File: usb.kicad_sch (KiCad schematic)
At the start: 6 parts, among them J4 USB_C_Receptacle_USB2.0, U4 PTN5150AHXMP

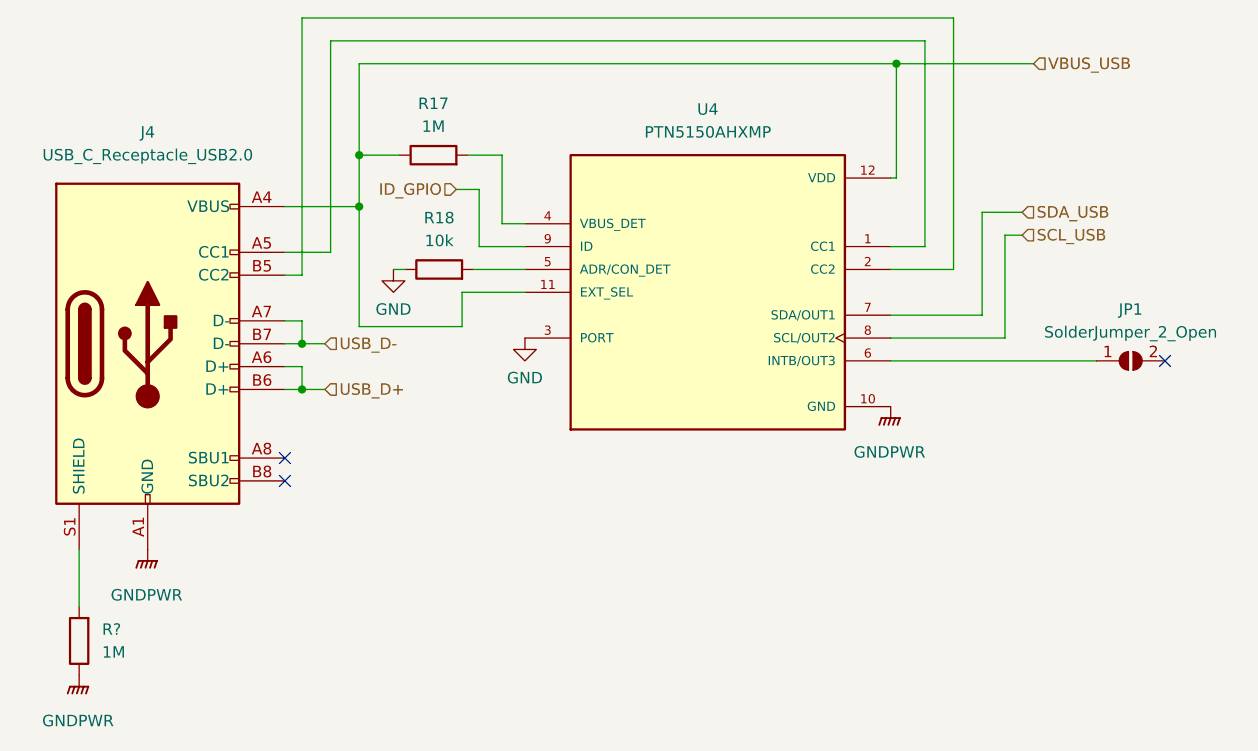
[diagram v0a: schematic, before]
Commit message: USB IC Removal
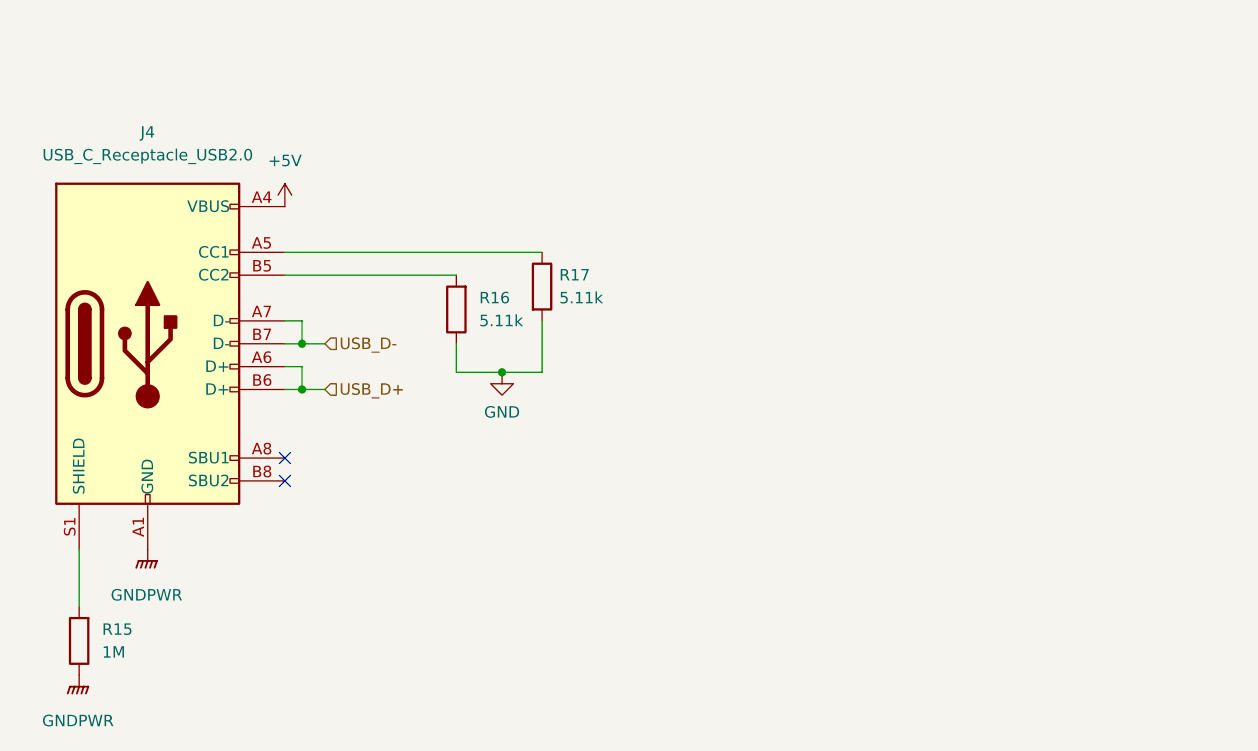
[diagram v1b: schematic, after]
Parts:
- removed JP1: SolderJumper_2_Open, Jumper:SolderJumper-2_P1.3mm_Open_Pad1.0x1.5mm, symbol Jumper:SolderJumper_2_Open
- removed R18: 10k, Resistor_SMD:R_0402_1005Metric, symbol Device:R
- removed U4: PTN5150AHXMP, JLCPCB:IC_PTN5150AHXMP, symbol JLCPCB:PTN5150AHXMP
- added R16: 5.11k, Resistor_SMD:R_0402_1005Metric, symbol Device:R
- R17: value 1M -> 5.11k
- gave numbers to parts that had none: 1
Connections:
- net GND: now also R17.2, R16.1
- net at J4.A5 (CC1): now also R17.1
- net at J4.B5 (CC2): now also R16.2
- net VBUS_USB renamed +5V
- net +5V: no longer R17.1
- no-connect marks 3 -> 2

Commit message: All Routed!
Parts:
- J6: renamed from J4; footprint JLCPCB:SOFNG_MC-311D -> lib_fp:SOFNG_MC-311D; MPN (none) -> C136423
- renumbered R15 to R17, R16 to R18, R17 to R19
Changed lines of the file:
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@@
   (symbol (lib_id "power:+5V") (at 128.905 72.39 0) (unit 1)
     (in_bom yes) (on_board yes) (fields_autoplaced)
-    (property "Reference" "#PWR033" (id 0) (at 128.905 76.2 0)
+    (property "Reference" "#PWR043" (id 0) (at 128.905 76.2 0)
       (effects (font (size 1.27 1.27)) hide)
     )
@@
   (symbol (lib_id "power:GND") (at 153.035 90.805 0) (unit 1)
     (in_bom yes) (on_board yes) (fields_autoplaced)
-    (property "Reference" "#PWR034" (id 0) (at 153.035 97.155 0)
+    (property "Reference" "#PWR044" (id 0) (at 153.035 97.155 0)
       (effects (font (size 1.27 1.27)) hide)
     )
@@
   (symbol (lib_id "Device:R") (at 106.045 120.65 180) (unit 1)
     (in_bom yes) (on_board yes) (fields_autoplaced)
-    (property "Reference" "R15" (id 0) (at 108.585 119.3799 0)
+    (property "Reference" "R17" (id 0) (at 108.585 119.3799 0)
       (effects (font (size 1.27 1.27)) (justify right))
     )
@@
   (symbol (lib_id "Device:R") (at 157.48 81.28 0) (unit 1)
     (in_bom yes) (on_board yes) (fields_autoplaced)
-    (property "Reference" "R17" (id 0) (at 159.385 80.0099 0)
+    (property "Reference" "R19" (id 0) (at 159.385 80.0099 0)
       (effects (font (size 1.27 1.27)) (justify left))
     )
@@
   (symbol (lib_id "power:GNDPWR") (at 113.665 110.49 0) (unit 1)
     (in_bom yes) (on_board yes) (fields_autoplaced)
-    (property "Reference" "#PWR032" (id 0) (at 113.665 115.57 0)
+    (property "Reference" "#PWR042" (id 0) (at 113.665 115.57 0)
       (effects (font (size 1.27 1.27)) hide)
     )
@@
   (symbol (lib_id "power:GNDPWR") (at 106.045 124.46 0) (unit 1)
     (in_bom yes) (on_board yes) (fields_autoplaced)
-    (property "Reference" "#PWR031" (id 0) (at 106.045 129.54 0)
+    (property "Reference" "#PWR041" (id 0) (at 106.045 129.54 0)
       (effects (font (size 1.27 1.27)) hide)
     )
@@
   (symbol (lib_id "Connector:USB_C_Receptacle_USB2.0") (at 113.665 87.63 0) (unit 1)
     (in_bom yes) (on_board yes) (fields_autoplaced)
-    (property "Reference" "J4" (id 0) (at 113.665 64.135 0))
+    (property "Reference" "J6" (id 0) (at 113.665 64.135 0))
     (property "Value" "USB_C_Receptacle_USB2.0" (id 1) (at 113.665 66.675 0))
-    (property "Footprint" "JLCPCB:SOFNG_MC-311D" (id 2) (at 117.475 87.63 0)
+    (property "Footprint" "lib_fp:SOFNG_MC-311D" (id 2) (at 117.475 87.63 0)
       (effects (font (size 1.27 1.27)) hide)
     )
     (property "Datasheet" "https://www.usb.org/sites/default/files/documents/usb_type-c.zip" (id 3) (at 117.475 87.63 0)
+      (effects (font (size 1.27 1.27)) hide)
+    )
+    (property "MPN" "C136423" (id 4) (at 113.665 87.63 0)
       (effects (font (size 1.27 1.27)) hide)
     )
@@
   (symbol (lib_id "Device:R") (at 147.955 83.82 180) (unit 1)
     (in_bom yes) (on_board yes) (fields_autoplaced)
-    (property "Reference" "R16" (id 0) (at 150.495 82.5499 0)
+    (property "Reference" "R18" (id 0) (at 150.495 82.5499 0)
       (effects (font (size 1.27 1.27)) (justify right))
     )

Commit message: New Audio
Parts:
- renumbered R17 to R15, R18 to R16, R19 to R17
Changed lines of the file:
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@@
   (symbol (lib_id "power:+5V") (at 128.905 72.39 0) (unit 1)
     (in_bom yes) (on_board yes) (fields_autoplaced)
-    (property "Reference" "#PWR043" (id 0) (at 128.905 76.2 0)
+    (property "Reference" "#PWR044" (id 0) (at 128.905 76.2 0)
       (effects (font (size 1.27 1.27)) hide)
     )
@@
   (symbol (lib_id "power:GND") (at 153.035 90.805 0) (unit 1)
     (in_bom yes) (on_board yes) (fields_autoplaced)
-    (property "Reference" "#PWR044" (id 0) (at 153.035 97.155 0)
+    (property "Reference" "#PWR045" (id 0) (at 153.035 97.155 0)
       (effects (font (size 1.27 1.27)) hide)
     )
@@
   (symbol (lib_id "Device:R") (at 106.045 120.65 180) (unit 1)
     (in_bom yes) (on_board yes) (fields_autoplaced)
-    (property "Reference" "R17" (id 0) (at 108.585 119.3799 0)
+    (property "Reference" "R15" (id 0) (at 108.585 119.3799 0)
       (effects (font (size 1.27 1.27)) (justify right))
     )
@@
   (symbol (lib_id "Device:R") (at 157.48 81.28 0) (unit 1)
     (in_bom yes) (on_board yes) (fields_autoplaced)
-    (property "Reference" "R19" (id 0) (at 159.385 80.0099 0)
+    (property "Reference" "R17" (id 0) (at 159.385 80.0099 0)
       (effects (font (size 1.27 1.27)) (justify left))
     )
@@
   (symbol (lib_id "power:GNDPWR") (at 113.665 110.49 0) (unit 1)
     (in_bom yes) (on_board yes) (fields_autoplaced)
-    (property "Reference" "#PWR042" (id 0) (at 113.665 115.57 0)
+    (property "Reference" "#PWR043" (id 0) (at 113.665 115.57 0)
       (effects (font (size 1.27 1.27)) hide)
     )
@@
   (symbol (lib_id "power:GNDPWR") (at 106.045 124.46 0) (unit 1)
     (in_bom yes) (on_board yes) (fields_autoplaced)
-    (property "Reference" "#PWR041" (id 0) (at 106.045 129.54 0)
+    (property "Reference" "#PWR042" (id 0) (at 106.045 129.54 0)
       (effects (font (size 1.27 1.27)) hide)
     )
@@
   (symbol (lib_id "Device:R") (at 147.955 83.82 180) (unit 1)
     (in_bom yes) (on_board yes) (fields_autoplaced)
-    (property "Reference" "R18" (id 0) (at 150.495 82.5499 0)
+    (property "Reference" "R16" (id 0) (at 150.495 82.5499 0)
       (effects (font (size 1.27 1.27)) (justify right))
     )

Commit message: First JLCPCB Ship!
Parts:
- added NT1: NetTie_2, NetTie:NetTie-2_SMD_Pad0.5mm, symbol Device:NetTie_2
- R15: MPN (none) -> C26083
- R16, R17: MPN (none) -> C25905
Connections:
- net GND: now also NT1.2
- net GNDPWR: now also NT1.1
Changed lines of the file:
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@@
 (kicad_sch (version 20211123) (generator eeschema)
   (paper "A4")
+  (junction (at 113.665 110.49) (diameter 0) (color 0 0 0 0)
+  )
   (junction (at 130.81 87.63) (diameter 0) (color 0 0 0 0)
   )
@@
   (no_connect (at 128.905 100.33))
   (no_connect (at 128.905 102.87))
+  (wire (pts (xy 118.745 112.395) (xy 118.745 110.49))
+    (stroke (width 0) (type default) (color 0 0 0 0))
+  )
   (wire (pts (xy 128.905 80.01) (xy 147.955 80.01))
     (stroke (width 0) (type default) (color 0 0 0 0))
@@
   )
   (wire (pts (xy 130.81 90.17) (xy 130.81 92.71))
+    (stroke (width 0) (type default) (color 0 0 0 0))
+  )
+  (wire (pts (xy 113.665 112.395) (xy 113.665 110.49))
     (stroke (width 0) (type default) (color 0 0 0 0))
   )
@@
   (symbol (lib_id "power:+5V") (at 128.905 72.39 0) (unit 1)
     (in_bom yes) (on_board yes) (fields_autoplaced)
-    (property "Reference" "#PWR040" (id 0) (at 128.905 76.2 0)
+    (property "Reference" "#PWR044" (id 0) (at 128.905 76.2 0)
       (effects (font (size 1.27 1.27)) hide)
     )
@@
     (pin "1")
   )
+  (symbol (lib_id "Device:NetTie_2") (at 116.205 110.49 0) (unit 1)
+    (in_bom yes) (on_board yes) (fields_autoplaced)
+    (property "Reference" "NT1" (id 0) (at 116.205 104.775 0))
+    (property "Value" "NetTie_2" (id 1) (at 116.205 107.315 0))
+    (property "Footprint" "NetTie:NetTie-2_SMD_Pad0.5mm" (id 2) (at 116.205 110.49 0)
+      (effects (font (size 1.27 1.27)) hide)
+    )
+    (property "Datasheet" "~" (id 3) (at 116.205 110.49 0)
+      (effects (font (size 1.27 1.27)) hide)
+    )
+    (pin "1")
+    (pin "2")
+  )
   (symbol (lib_id "power:GND") (at 153.035 90.805 0) (unit 1)
     (in_bom yes) (on_board yes) (fields_autoplaced)
-    (property "Reference" "#PWR041" (id 0) (at 153.035 97.155 0)
+    (property "Reference" "#PWR045" (id 0) (at 153.035 97.155 0)
       (effects (font (size 1.27 1.27)) hide)
     )
@@
       (effects (font (size 1.27 1.27)) hide)
     )
+    (property "MPN" "C26083" (id 4) (at 106.045 120.65 0)
+      (effects (font (size 1.27 1.27)) hide)
+    )
     (pin "1")
     (pin "2")
@@
       (effects (font (size 1.27 1.27)) hide)
     )
+    (property "MPN" "C25905" (id 4) (at 157.48 81.28 0)
+      (effects (font (size 1.27 1.27)) hide)
+    )
     (pin "1")
     (pin "2")
   )
-  (symbol (lib_id "power:GNDPWR") (at 113.665 110.49 0) (unit 1)
-    (in_bom yes) (on_board yes) (fields_autoplaced)
-    (property "Reference" "#PWR039" (id 0) (at 113.665 115.57 0)
-      (effects (font (size 1.27 1.27)) hide)
-    )
-    (property "Value" "GNDPWR" (id 1) (at 113.538 115.57 0))
-    (property "Footprint" "" (id 2) (at 113.665 111.76 0)
-      (effects (font (size 1.27 1.27)) hide)
-    )
-    (property "Datasheet" "" (id 3) (at 113.665 111.76 0)
+  (symbol (lib_id "power:GNDPWR") (at 113.665 112.395 0) (unit 1)
+    (in_bom yes) (on_board yes) (fields_autoplaced)
+    (property "Reference" "#PWR042" (id 0) (at 113.665 117.475 0)
+      (effects (font (size 1.27 1.27)) hide)
+    )
+    (property "Value" "GNDPWR" (id 1) (at 113.538 117.475 0))
+    (property "Footprint" "" (id 2) (at 113.665 113.665 0)
+      (effects (font (size 1.27 1.27)) hide)
+    )
+    (property "Datasheet" "" (id 3) (at 113.665 113.665 0)
       (effects (font (size 1.27 1.27)) hide)
     )
@@
   (symbol (lib_id "power:GNDPWR") (at 106.045 124.46 0) (unit 1)
     (in_bom yes) (on_board yes) (fields_autoplaced)
-    (property "Reference" "#PWR038" (id 0) (at 106.045 129.54 0)
+    (property "Reference" "#PWR041" (id 0) (at 106.045 129.54 0)
       (effects (font (size 1.27 1.27)) hide)
     )
@@
     (pin "S1")
   )
+  (symbol (lib_id "power:GND") (at 118.745 112.395 0) (unit 1)
+    (in_bom yes) (on_board yes) (fields_autoplaced)
+    (property "Reference" "#PWR043" (id 0) (at 118.745 118.745 0)
+      (effects (font (size 1.27 1.27)) hide)
+    )
+    (property "Value" "GND" (id 1) (at 118.745 116.84 0))
+    (property "Footprint" "" (id 2) (at 118.745 112.395 0)
+      (effects (font (size 1.27 1.27)) hide)
+    )
+    (property "Datasheet" "" (id 3) (at 118.745 112.395 0)
+      (effects (font (size 1.27 1.27)) hide)
+    )
+    (pin "1")
+  )
   (symbol (lib_id "Device:R") (at 147.955 83.82 180) (unit 1)
     (in_bom yes) (on_board yes) (fields_autoplaced)
@@
       (effects (font (size 1.27 1.27)) hide)
     )
+    (property "MPN" "C25905" (id 4) (at 147.955 83.82 0)
+      (effects (font (size 1.27 1.27)) hide)
+    )
